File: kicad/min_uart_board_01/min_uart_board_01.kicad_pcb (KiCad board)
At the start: 2 copper layers, 97 x 34.5 mm, 13 parts, among them J1 DIN41612_02x32_AC, J2 UART1, J3 UART2, U10 TL28L92FR, U13 74AHC1G32, Y1 Crystal 3.6864MHz

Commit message: pinout artwork
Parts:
- moved C2 5.08 mm to (89.4, 84.9)
- moved C1 4.57 mm to (92.7, 84.9)
- moved Y1 3.90 mm to (96.5, 81.0)
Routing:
- net /UART_X1: track 27.8 -> 23.0 mm
- net /UART_X2: track 22.8 -> 18.6 mm
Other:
- outline, holes or cut-outs redrawn
- board text added: "1"
- board text added: "2"
- board text added: "CTS"
- board text added: "GND"
- board text added: "NC"
- board text added: "RTS"
- board text added: "RX"
- board text added: "TX"
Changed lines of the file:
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@@
 		(tags "Through hole angled pin header THT 2x03 2.54mm double row")
 		(property "Reference" "J2"
-			(at -3.048 1.778 0)
+			(at 1.016 7.62 0)
 			(layer "F.SilkS")
 			(effects
@@
 		(tags "Through hole angled pin header THT 2x03 2.54mm double row")
 		(property "Reference" "J3"
-			(at -2.794 0 0)
+			(at 0.762 8.89 0)
 			(layer "F.SilkS")
 			(effects
@@
 	(footprint "Capacitor_THT:C_Disc_D4.7mm_W2.5mm_P5.00mm"
 		(layer "F.Cu")
-		(at 84.328 84.836 -90)
+		(at 89.408 84.916 -90)
 		(descr "C, Disc series, Radial, pin pitch=5.00mm, diameter*width=4.7*2.5mm^2, Capacitor, http://www.vishay.com/docs/45233/krseries.pdf")
 		(tags "C Disc series Radial pin pitch 5.00mm diameter 4.7mm width 2.5mm Capacitor")
@@
 	(footprint "Crystal:Crystal_HC49-4H_Vertical"
 		(layer "F.Cu")
-		(at 93.308 83.312)
+		(at 96.466 81.026)
 		(descr "Crystal THT HC-49-4H http://5hertz.com/pdfs/04404_D.pdf")
 		(tags "THT crystalHC-49-4H")
 		(property "Reference" "Y1"
-			(at -4.662 -1.524 0)
+			(at -4.518 0.254 0)
 			(layer "F.SilkS")
 			(effects
@@
 	(footprint "Capacitor_THT:C_Disc_D4.7mm_W2.5mm_P5.00mm"
 		(layer "F.Cu")
-		(at 88.138 84.836 -90)
+		(at 92.71 84.916 -90)
 		(descr "C, Disc series, Radial, pin pitch=5.00mm, diameter*width=4.7*2.5mm^2, Capacitor, http://www.vishay.com/docs/45233/krseries.pdf")
 		(tags "C Disc series Radial pin pitch 5.00mm diameter 4.7mm width 2.5mm Capacitor")
@@
 		(tags "DIN 41612 IEC 60603 C")
 		(property "Reference" "J1"
-			(at -4.572 2.54 0)
+			(at 0 -2.27 0)
 			(layer "F.SilkS")
 			(effects
@@
 		)
 	)
+	(gr_circle
+		(center 132.842 101.092)
+		(end 133.096 100.838)
+		(stroke
+			(width 0.1)
+			(type default)
+		)
+		(fill no)
+		(layer "F.SilkS")
+	)
+	(gr_circle
+		(center 132.842 99.06)
+		(end 133.096 98.806)
+		(stroke
+			(width 0.1)
+			(type default)
+		)
+		(fill no)
+		(layer "F.SilkS")
+	)
+	(gr_circle
+		(center 131.826 99.06)
+		(end 132.08 98.806)
+		(stroke
+			(width 0.1)
+			(type default)
+		)
+		(fill no)
+		(layer "F.SilkS")
+	)
+	(gr_circle
+		(center 132.842 103.124)
+		(end 133.096 102.87)
+		(stroke
+			(width 0.1)
+			(type default)
+		)
+		(fill no)
+		(layer "F.SilkS")
+	)
+	(gr_circle
+		(center 131.826 103.124)
+		(end 132.08 102.87)
+		(stroke
+			(width 0.1)
+			(type default)
+		)
+		(fill no)
+		(layer "F.SilkS")
+	)
+	(gr_rect
+		(start 131.064 98.044)
+		(end 133.604 104.14)
+		(stroke
+			(width 0.1)
+			(type default)
+		)
+		(fill no)
+		(layer "F.SilkS")
+	)
+	(gr_circle
+		(center 131.826 101.092)
+		(end 132.08 100.838)
+		(stroke
+			(width 0.1)
+			(type default)
+		)
+		(fill no)
+		(layer "F.SilkS")
+	)
 	(gr_line
 		(start 137.16 77.47)
@@
 	(gr_line
 		(start 40.132 96.52)
-		(end 69.85 96.52)
+		(end 73.66 96.52)
 		(stroke
 			(width 0.05)
@@
 	)
 	(gr_line
-		(start 88.9 77.47)
+		(start 92.71 77.47)
 		(end 137.16 77.47)
 		(stroke
@@
 	)
 	(gr_line
-		(start 69.85 96.52)
-		(end 88.9 77.47)
+		(start 73.66 96.52)
+		(end 92.71 77.47)
 		(stroke
 			(width 0.05)
@@
 		(layer "Edge.Cuts")
 	)
+	(gr_text "2"
+		(at 120.65 92.964 0)
+		(layer "F.SilkS")
+		(effects
+			(font
+				(size 1 1)
+				(thickness 0.1)
+			)
+			(justify left bottom)
+		)
+	)
+	(gr_text "TX"
+		(at 129.032 103.632 0)
+		(layer "F.SilkS")
+		(effects
+			(font
+				(size 1 1)
+				(thickness 0.1)
+			)
+			(justify left bottom)
+		)
+	)
+	(gr_text "RX"
+		(at 128.778 101.6 0)
+		(layer "F.SilkS")
+		(effects
+			(font
+				(size 1 1)
+				(thickness 0.1)
+			)
+			(justify left bottom)
+		)
+	)
+	(gr_text "CTS"
+		(at 133.858 103.632 0)
+		(layer "F.SilkS")
+		(effects
+			(font
+				(size 1 1)
+				(thickness 0.1)
+			)
+			(justify left bottom)
+		)
+	)
+	(gr_text "NC"
+		(at 134.112 99.568 0)
+		(layer "F.SilkS")
+		(effects
+			(font
+				(size 1 1)
+				(thickness 0.1)
+			)
+			(justify left bottom)
+		)
+	)
+	(gr_text "RTS"
+		(at 133.858 101.6 0)
+		(layer "F.SilkS")
+		(effects
+			(font
+				(size 1 1)
+				(thickness 0.1)
+			)
+			(justify left bottom)
+		)
+	)
+	(gr_text "GND"
+		(at 127.762 99.568 0)
+		(layer "F.SilkS")
+		(effects
+			(font
+				(size 1 1)
+				(thickness 0.1)
+			)
+			(justify left bottom)
+		)
+	)
+	(gr_text "1"
+		(at 120.65 83.566 0)
+		(layer "F.SilkS")
+		(effects
+			(font
+				(size 1 1)
+				(thickness 0.1)
+			)
+			(justify left bottom)
+		)
+	)
 	(segment
 		(start 116.7875 89.09)
@@
 	)
 	(segment
-		(start 91.44 91.694)
-		(end 101.854 81.28)
+		(start 107.1 81.911768)
+		(end 107.1 82.6025)
 		(width 0.2)
 		(layer "F.Cu")
@@
 	)
 	(segment
-		(start 106.468232 81.28)
-		(end 107.1 81.911768)
+		(start 50.8 101.6)
+		(end 53.34 99.06)
 		(width 0.2)
 		(layer "F.Cu")
@@
 	)
 	(segment
-		(start 53.34 99.06)
-		(end 73.914 99.06)
+		(start 92.71 91.694)
+		(end 103.124 81.28)
 		(width 0.2)
 		(layer "F.Cu")
@@
 	)
 	(segment
-		(start 107.1 81.911768)
-		(end 107.1 82.6025)
+		(start 53.34 99.06)
+		(end 73.914 99.06)
 		(width 0.2)
 		(layer "F.Cu")
@@
 	)
 	(segment
-		(start 81.28 91.694)
-		(end 91.44 91.694)
+		(start 103.124 81.28)
+		(end 106.468232 81.28)
 		(width 0.2)
 		(layer "F.Cu")
@@
 	)
 	(segment
-		(start 50.8 101.6)
-		(end 53.34 99.06)
+		(start 106.468232 81.28)
+		(end 107.1 81.911768)
 		(width 0.2)
 		(layer "F.Cu")
@@
 	)
 	(segment
-		(start 73.914 99.06)
-		(end 81.28 91.694)
+		(start 81.28 91.694)
+		(end 92.71 91.694)
 		(width 0.2)
 		(layer "F.Cu")
@@
 	)
 	(segment
-		(start 101.854 81.28)
-		(end 106.468232 81.28)
+		(start 73.914 99.06)
+		(end 81.28 91.694)
 		(width 0.2)
 		(layer "F.Cu")
@@
 	)
 	(segment
-		(start 96.664 84.836)
-		(end 88.138 84.836)
+		(start 107.9 81.665001)
+		(end 107.9 82.6025)
 		(width 0.2)
 		(layer "F.Cu")
@@
 	)
 	(segment
-		(start 100.728 80.772)
-		(end 98.188 83.312)
+		(start 101.346 81.026)
+		(end 102.096 80.276)
 		(width 0.2)
 		(layer "F.Cu")
@@
 	)
 	(segment
-		(start 98.188 83.312)
-		(end 96.664 84.836)
+		(start 106.510999 80.276)
+		(end 107.9 81.665001)
 		(width 0.2)
 		(layer "F.Cu")
@@
 	)
 	(segment
-		(start 107.9 81.665001)
-		(end 107.006999 80.772)
+		(start 92.71 84.916)
+		(end 97.456 84.916)
 		(width 0.2)
 		(layer "F.Cu")
@@
 	)
 	(segment
-		(start 107.006999 80.772)
-		(end 100.728 80.772)
+		(start 97.456 84.916)
+		(end 101.346 81.026)
 		(width 0.2)
 		(layer "F.Cu")
@@
 	)
 	(segment
-		(start 107.9 82.6025)
-		(end 107.9 81.665001)
+		(start 102.096 80.276)
+		(end 106.510999 80.276)
 		(width 0.2)
 		(layer "F.Cu")
@@
 	)
 	(segment
-		(start 93.308 83.312)
-		(end 96.356 80.264)
+		(start 93.298 81.026)
+		(end 96.466 81.026)
 		(width 0.2)
 		(layer "F.Cu")
@@
 	)
 	(segment
-		(start 107.298999 80.264)
-		(end 108.7 81.665001)
+		(start 89.408 84.916)
+		(end 93.298 81.026)
 		(width 0.2)
 		(layer "F.Cu")
@@
 	)
 	(segment
-		(start 85.852 83.312)
-		(end 93.308 83.312)
+		(start 108.7 81.665001)
+		(end 108.7 82.6025)
 		(width 0.2)
 		(layer "F.Cu")
@@
 	)
 	(segment
-		(start 96.356 80.264)
-		(end 107.298999 80.264)
+		(start 106.959999 79.925)
+		(end 108.7 81.665001)
 		(width 0.2)
 		(layer "F.Cu")
@@
 	)
 	(segment
-		(start 108.7 81.665001)
-		(end 108.7 82.6025)
+		(start 97.567 79.925)
+		(end 106.959999 79.925)
 		(width 0.2)
 		(layer "F.Cu")
@@
 	)
 	(segment
-		(start 84.328 84.836)
-		(end 85.852 83.312)
+		(start 96.466 81.026)
+		(end 97.567 79.925)
 		(width 0.2)
 		(layer "F.Cu")
@@
 	)
 	(segment
-		(start 82.55 94.712)
-		(end 83.312 94.712)
+		(start 83.312 94.712)
+		(end 85.501 92.523)
 		(width 0.2)
 		(layer "F.Cu")
@@
 	)
 	(segment
-		(start 83.312 94.712)
-		(end 85.501 92.523)
+		(start 82.55 94.712)
+		(end 83.312 94.712)
 		(width 0.2)
 		(layer "F.Cu")

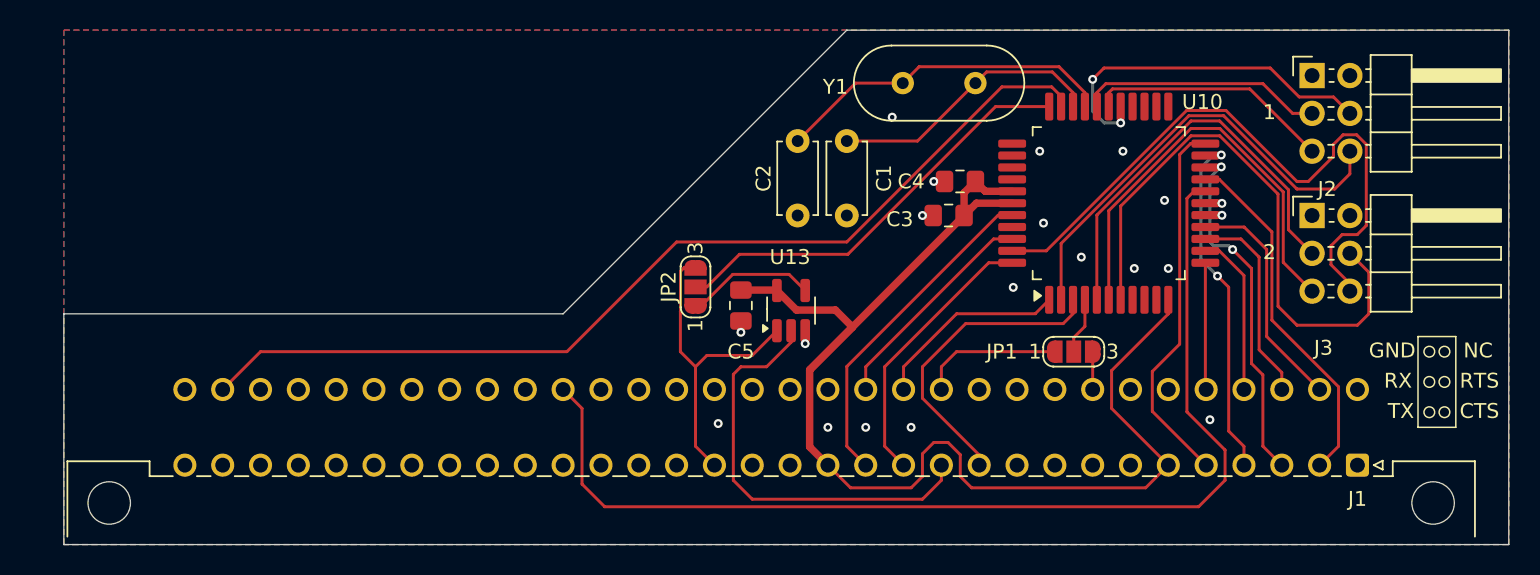
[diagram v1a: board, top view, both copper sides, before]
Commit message: restoring min uart board from backup... some horrible mess happened
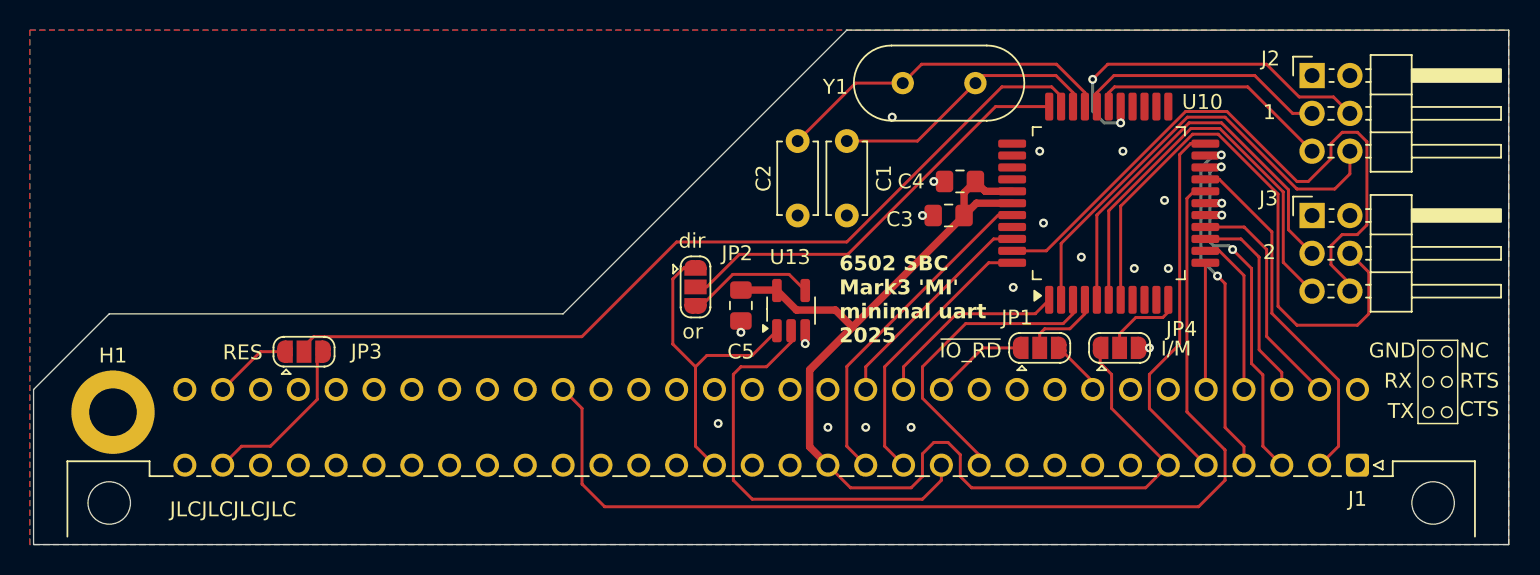
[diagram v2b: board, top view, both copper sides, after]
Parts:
- added H1: GND, MountingHole:MountingHole_3.2mm_M3_DIN965_Pad, F.Cu at (43.4, 103.1)
- added JP3: SolderJumper_3_Open, Jumper:SolderJumper-3_P1.3mm_Open_RoundedPad1.0x1.5mm, F.Cu at (56.3, 99.1)
- added JP4: SolderJumper_3_Open, Jumper:SolderJumper-3_P1.3mm_Open_RoundedPad1.0x1.5mm, F.Cu at (111.0, 98.8)
- JP1, JP2: footprint Jumper:SolderJumper-3_P1.3mm_Open_RoundedPad1.0x1.5mm_NumberLabels -> Jumper:SolderJumper-3_P1.3mm_Open_RoundedPad1.0x1.5mm
- moved JP1 2.30 mm to (105.7, 98.8)
- turned JP2 to -90 degrees
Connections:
- JP2 pad 1: Net-(JP2-A) -> /~{IOEN_02_UART}
- JP2 pad 3: /~{IOEN_02_UART} -> Net-(JP2-B)
- U10 pad 11: VCC -> Net-(JP4-C)
- U10 pad 32: /RES -> Net-(JP3-C)
- U13 pad 4: Net-(JP2-A) -> Net-(JP2-B)
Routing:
- net /RES: track 65.7 -> 5.21 mm
- net Net-(JP3-C): track 0.00 -> 59.4 mm
- net /~{RES}: track 0.00 -> 11.6 mm
- net Net-(JP2-B): track 0.00 -> 8.70 mm
- net Net-(JP2-A): track 8.70 -> 0.00 mm
- net Net-(JP4-C): track 0.00 -> 5.64 mm
- net VCC: track 85.8 -> 81.2 mm
- net /~{IO_RD}: track 9.53 -> 6.46 mm
- net Net-(JP1-C): track 3.79 -> 5.48 mm
- net /PLD_O7: track 2.55 -> 3.73 mm
- net GND: track 5.30 -> 5.98 mm
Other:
- board size 97 x 34.5 mm -> 99.1 x 34.5 mm
- board text added: "6502 SBC Mark3 'MI' minimal uart 2025"
- board text added: "I/M"
- board text added: "JLCJLCJLCJLC"
- board text added: "RES"
- board text added: "dir"
- board text added: "or"
- board text added: "~{IO_RD}"

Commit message: min uart v1.1 -> almost all rounting on front layer
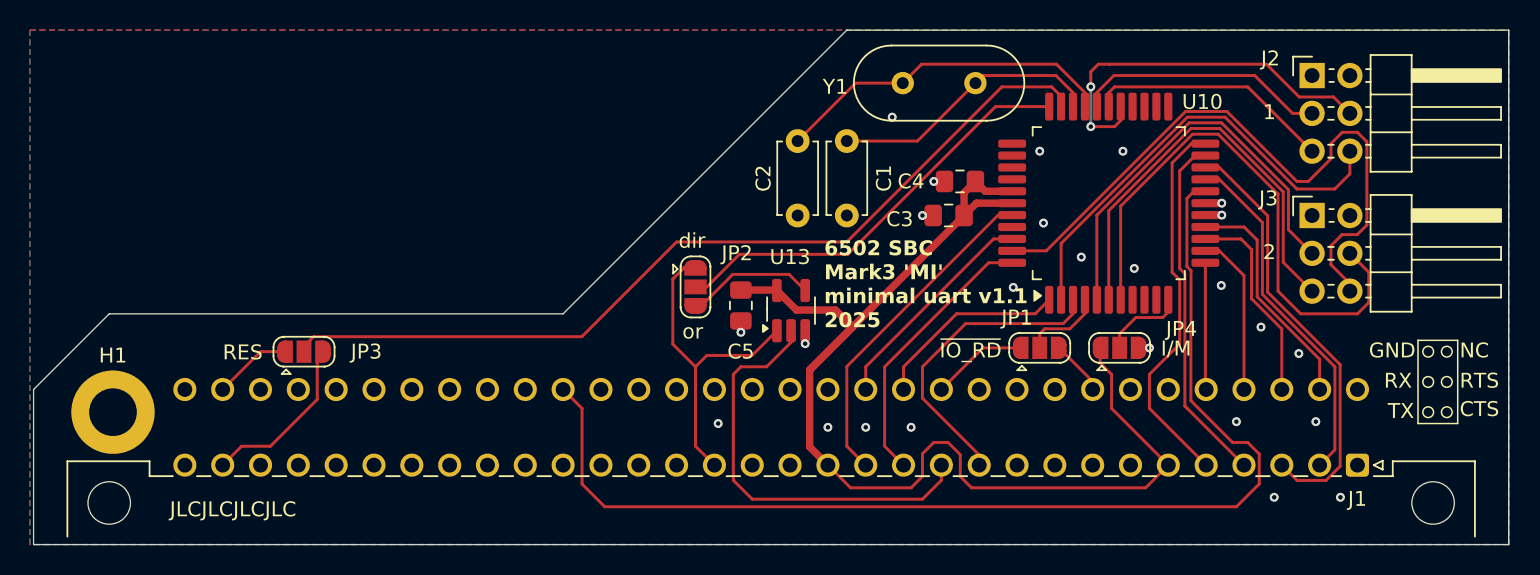
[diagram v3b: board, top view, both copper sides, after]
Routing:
- net /DB4: track 24.3 -> 29.1 mm, vias 2 -> 0
- net /~{IRQ}: track 72.8 -> 76.8 mm
- net /RTS_D1: track 23.4 -> 25.8 mm
- net /RTS_D2: track 39.6 -> 37.9 mm
- net /DB2: track 24.0 -> 23.7 mm, vias 2 -> 0
- net GND: vias 20 -> 25
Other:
- board text added: "6502 SBC Mark3 'MI' minimal uart v1.1 2025"
- board text removed: "6502 SBC Mark3 'MI' minimal uart 2025"
